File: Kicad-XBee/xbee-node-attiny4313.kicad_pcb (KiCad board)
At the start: 2 copper layers, 58.5 x 58.5 mm, 23 parts, among them P1 Program, P2 XBee Adaptor, P3 Led, P4 Battery, Q1 S1133, Q2 S9014, Q3 2N7000, U1 ATTINY4313-S, U2 LM358, U3 TPS77033

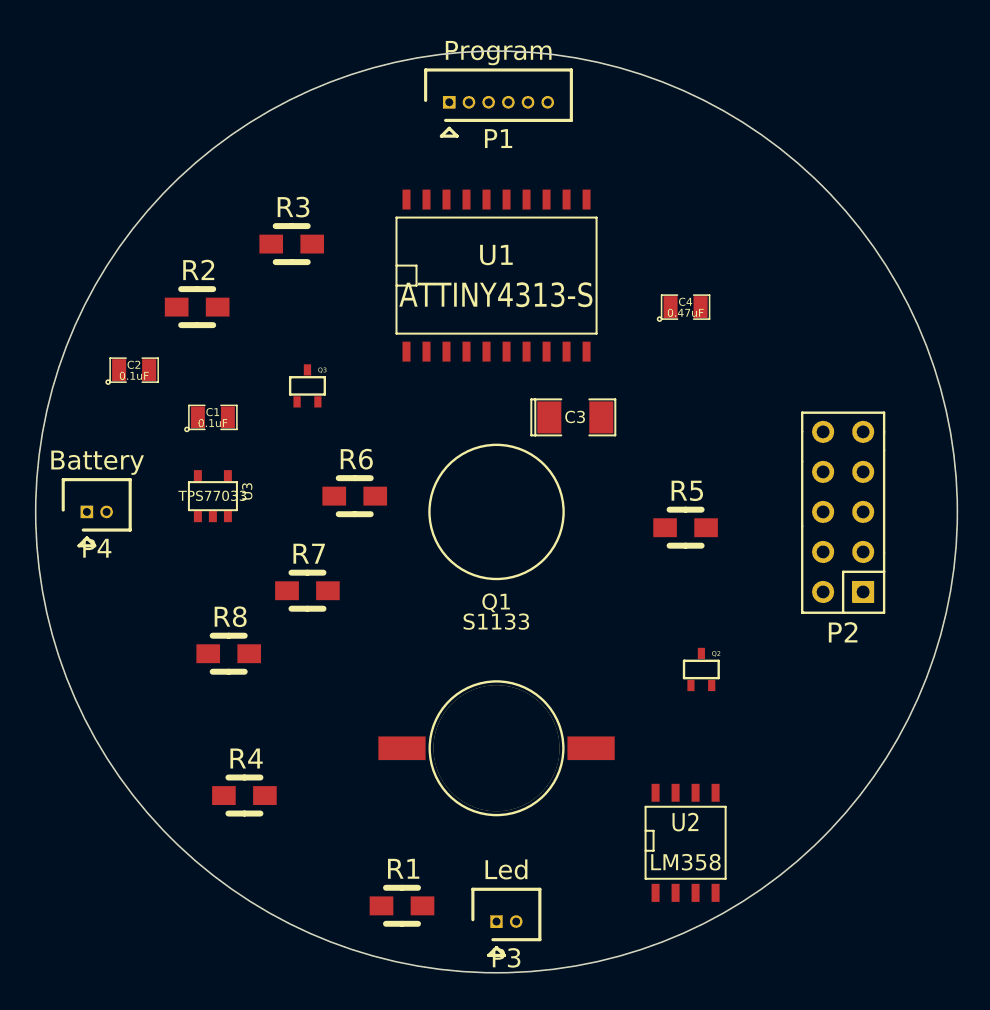
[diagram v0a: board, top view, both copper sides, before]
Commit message: Update to firmware to make XBee wake and successfully communicate to coorsinator. More work on PCB to complette layout and add tracks.
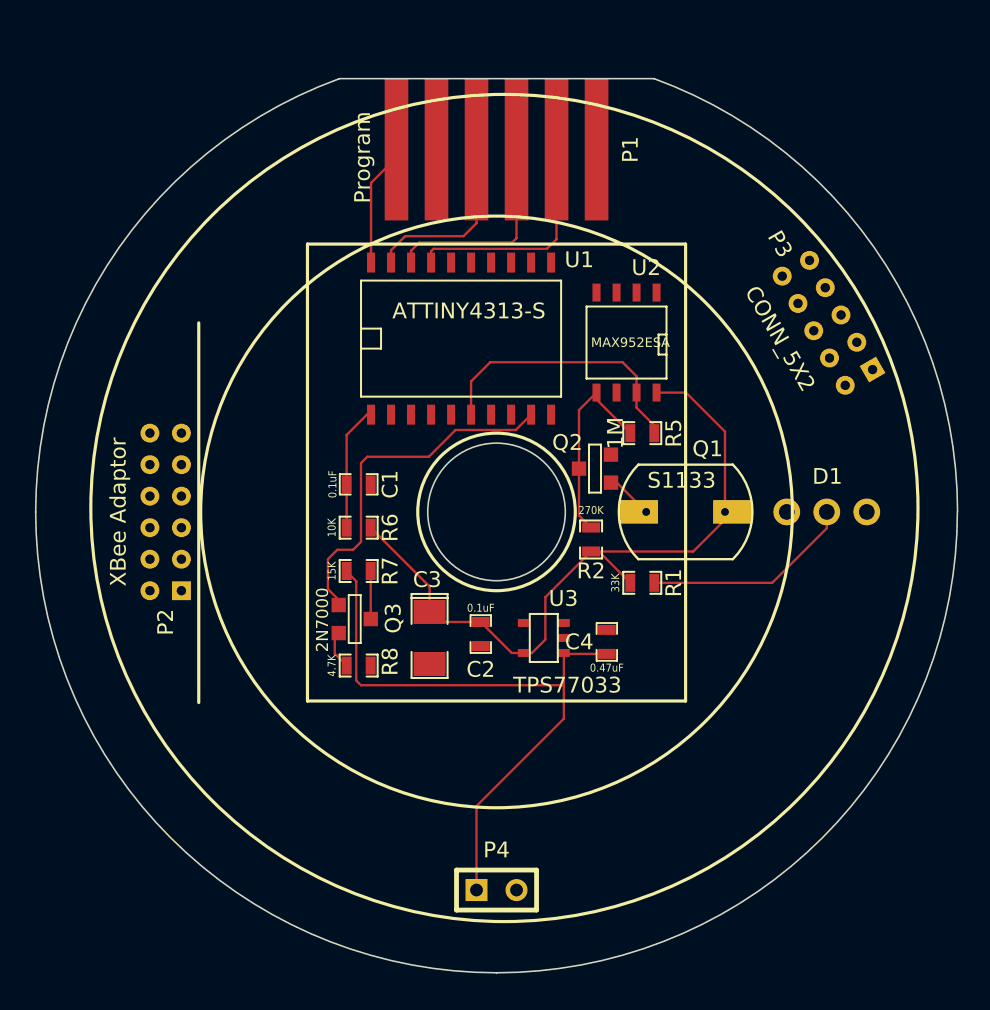
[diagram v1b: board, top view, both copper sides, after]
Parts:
- removed ?: , PhotoDiode:Mounting-Hole_8.5
- removed R3: 120K, Resistors_SMD:Resistor_SMD0805_HandSoldering
- removed R4: 22K, Resistors_SMD:Resistor_SMD0805_HandSoldering
- added D1: APD3224ZGC-F01, PhotoDiode:LED-Mount, F.Cu at (223.5, 100.0)
- C1, C2, C4: footprint SMD_Packages:SM0805 -> SMD_Packages:SM0603_Capa
- P1: footprint Connectors_Serial_MOLEX:Connector_Molex_PicoBlade_53047-0610 -> PhotoDiode:edge_conn_6_pin
- P2: footprint imciner2:CONN_2x5 -> PhotoDiode:pin_header_2mm_2x6
- P3: value Led -> CONN_5X2; footprint Connectors_Serial_MOLEX:Connector_Molex_PicoBlade_53047-0210 -> PhotoDiode:pin_header_2mm_2x5
- P4: footprint Connectors_Serial_MOLEX:Connector_Molex_PicoBlade_53047-0210 -> Connect:SIL-2
- Q1: footprint PhotoDiode:S1133 -> PhotoDiode:S1133TH
- Q2: footprint Transistors_SMD:sc70 -> SMD_Packages:SOT23EBC
- Q3: footprint Transistors_SMD:sc70 -> SMD_Packages:SOT23GDS
- R1, R5, R6, R7, R8: footprint Resistors_SMD:Resistor_SMD0805_HandSoldering -> SMD_Packages:SM0603_Resistor
- R2: value 100K -> 270K; footprint Resistors_SMD:Resistor_SMD0805_HandSoldering -> SMD_Packages:SM0603_Resistor
- U2: value LM358 -> MAX952ESA
- moved P3 43.4 mm to (221.0, 88.0), turned to 120 degrees
- moved P2 43.0 mm to (179.0, 100.0), turned to 90 degrees
- moved P4 35.4 mm to (200.0, 124.0)
- moved U2 32.0 mm to (208.2, 89.2), turned to 180 degrees
- moved R2 29.0 mm to (206.0, 101.8), turned to 90 degrees
- moved C2 27.7 mm to (199.0, 107.8), turned to 270 degrees
- moved R1 25.6 mm to (209.2, 104.5)
- moved U3 22.8 mm to (203.0, 108.0), turned to 90 degrees
- moved C4 21.8 mm to (207.0, 108.2), turned to 90 degrees
- moved C3 16.8 mm to (195.8, 108.0), turned to 270 degrees
- moved Q3 15.1 mm to (191.0, 106.8), turned to 90 degrees
- moved Q2 14.4 mm to (206.2, 97.2), turned to 270 degrees
- moved Q1 13.9 mm to (212.0, 100.0)
- moved C1 10.2 mm to (191.2, 98.2)
- moved R8 8.28 mm to (191.2, 109.8)
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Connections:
- net Net-(P2-Pad7) renamed /Bootloader
- C1 pad 1: Net-(C1-Pad1) -> /Reset
- C2 pad 1: Net-(C2-Pad1) -> VDD
- C3 pad 1: Net-(C3-Pad1) -> VDD
- C4 pad 1: Net-(C4-Pad1) -> /VBatt
- P1 pad 5: Net-(C1-Pad1) -> /Reset
- P2 pad 10: Net-(P2-Pad10) -> /Xbee-Reset
- P2 pad 2: Net-(P2-Pad2) -> /Sleep-Rq
- P2 pad 3: Net-(P2-Pad3) -> /Rx
- P2 pad 4: Net-(P2-Pad4) -> /CTS
- P2 pad 5: Net-(P2-Pad5) -> /Tx
- P2 pad 6: Net-(P2-Pad6) -> /RTS
- P2 pad 8: Net-(P2-Pad8) -> /On/Sleep
- P2 pad 9: GND -> /Reset
- P3 pad 1: Net-(P3-Pad1) -> /Rx
- P3 pad 2: GND -> /Sleep-Rq
- P4 pad 1: Net-(P4-Pad1) -> /VBatt
- Q2 pad 3: Net-(Q1-Pad3) -> Net-(Q2-Pad3)
- R1 pad 1: Net-(P3-Pad1) -> VDD
- R1 pad 2: Net-(P4-Pad1) -> Net-(D1-Pad2)
- R2 pad 2: Net-(Q1-Pad3) -> Net-(Q2-Pad3)
- R5 pad 1: Net-(R3-Pad2) -> Net-(Q2-Pad3)
- R5 pad 2: Net-(R5-Pad2) -> Net-(P3-Pad5)
- R6 pad 1: Net-(C1-Pad1) -> /Reset
- R7 pad 1: Net-(P4-Pad1) -> /VBatt
- U1 pad 1: Net-(C1-Pad1) -> /Reset
- U1 pad 13: Net-(P2-Pad6) -> /On/Sleep
- U1 pad 14: Net-(U1-Pad14) -> /Xbee-Reset
- U1 pad 15: Net-(P2-Pad2) -> /Sleep-Rq
- U1 pad 2: Net-(P2-Pad3) -> /Rx
- U1 pad 3: Net-(P2-Pad5) -> /Tx
- U1 pad 4: Net-(U1-Pad4) -> /CTS
- U1 pad 5: Net-(U1-Pad5) -> /RTS
- U1 pad 6: Net-(R5-Pad2) -> Net-(P3-Pad5)
- U2 pad 1: Net-(R5-Pad2) -> Net-(U2-Pad1)
- U2 pad 2: Net-(Q1-Pad3) -> GND
- U2 pad 3: Net-(R3-Pad2) -> GND
- U2 pad 5: (no net) -> Net-(Q2-Pad3)
- U2 pad 6: (no net) -> Net-(U2-Pad6)
- U2 pad 7: (no net) -> Net-(P3-Pad5)
- U3 pad 1: Net-(P4-Pad1) -> /VBatt
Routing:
- net VDD: track 0.00 -> 53.4 mm
- net /VBatt: track 0.00 -> 40.6 mm
- net Net-(Q3-PadG): track 0.00 -> 22.8 mm
- net Net-(P3-Pad5): track 0.00 -> 17.6 mm
- net Net-(P1-Pad2): track 0.00 -> 14.2 mm
- net Net-(D1-Pad2): track 0.00 -> 13.4 mm
- net Net-(P1-Pad3): track 0.00 -> 12.9 mm
- net Net-(Q2-Pad3): track 0.00 -> 12.8 mm
- net Net-(P1-Pad4): track 0.00 -> 11.6 mm
- net /Reset: track 0.00 -> 7.97 mm
- net Net-(Q3-PadD): track 0.00 -> 3.05 mm
- net Net-(Q1-Pad1): track 0.00 -> 3.00 mm
- net Net-(Q3-PadS): track 0.00 -> 2.42 mm
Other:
- board size 58.5 x 58.5 mm -> 58.5 x 56.8 mm
- net class Default: clearance 0.254 -> 0.15; trace_width 0.254 -> 0.15
- net class Power added: clearance 0.15, trace_width 0.3, via_dia 0.889, via_drill 0.635
- rule trace_clearance: 0.254 -> 0.15
- rule trace_min: 0.254 -> 0.15
- rule via_min_drill: 0.508 -> 0.3
